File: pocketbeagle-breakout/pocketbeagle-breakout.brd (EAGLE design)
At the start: 102.9 x 68.6 mm, 91 parts, among them J30 4-1734592-04-1734592-0, J31 4-1734592-04-1734592-0, J5 POWER_JACKSLT, P1 BCS-118-L-D-TE, P1IN BCS-118-L-D-TE, P2 BCS-118-L-D-TE, P2IN BCS-118-L-D-TE, U1 TCAN330

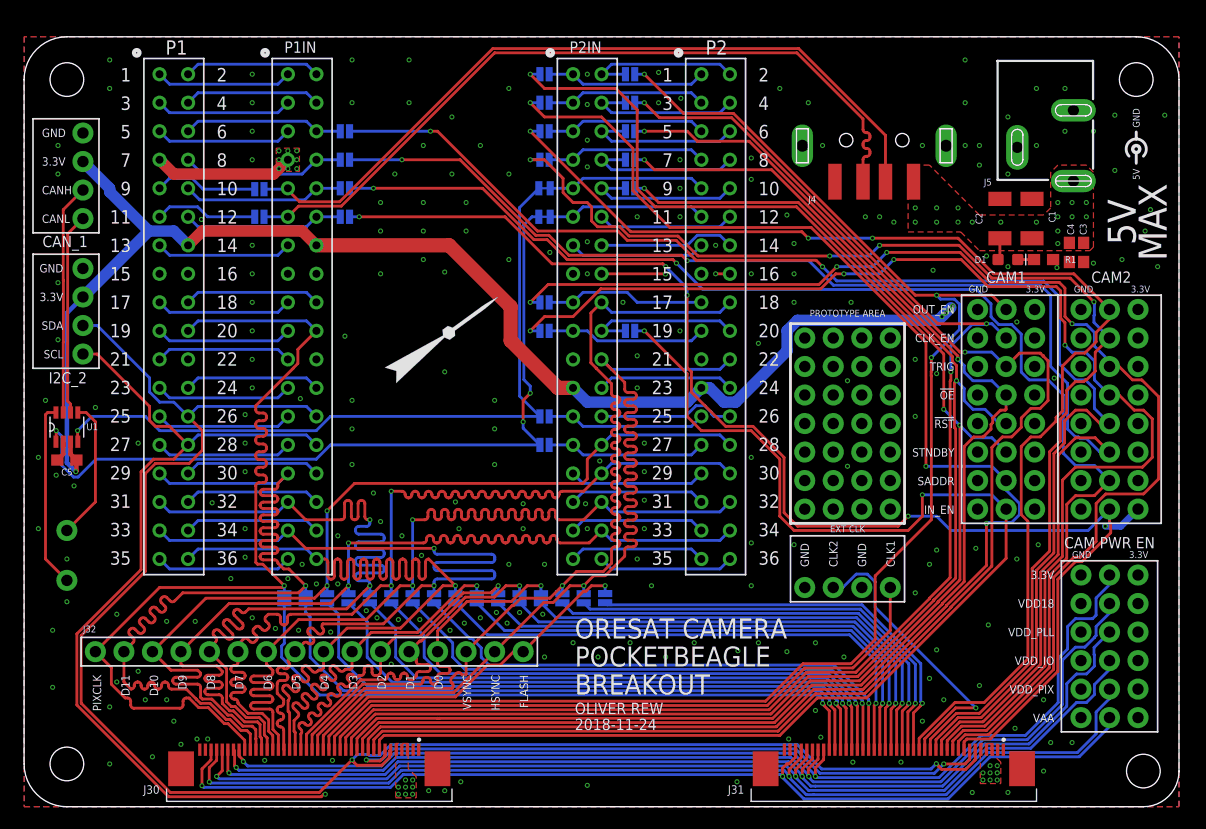
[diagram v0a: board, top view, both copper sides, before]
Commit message: address review comments: used round hole on USB and power, changed CAN connector, other small stuff
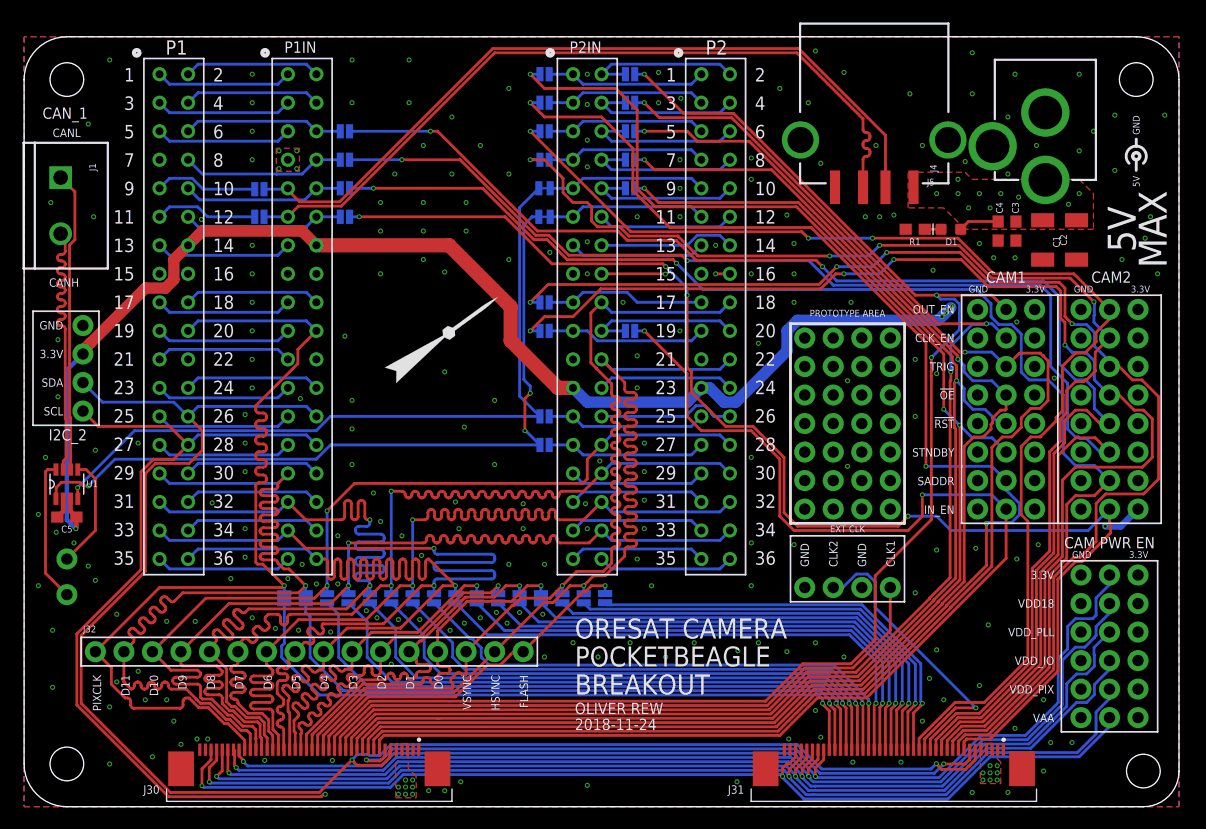
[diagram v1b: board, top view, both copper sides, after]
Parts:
- removed J29: (no value), SparkFun-Connectors:1X04_NO_SILK
- added J1: (no value), SparkFun-Connectors:SCREWTERMINAL-5MM-2
- J4: value (none) -> USB_A_SMT_FEMALE; device J-WURTH-USB-A-FEMALE-629104151021:629104151021 -> SparkFun-Connectors:USB-A-S-SILK-FEMALE
- J5: value POWER_JACKSLT -> POWER_JACK; device SparkFun-Connectors:POWER_JACK_SLOT -> SparkFun-Connectors:POWER_JACK_PTH
- moved R1 11.7 mm to (79.4, 51.4), turned to 180 degrees
- moved C4 6.63 mm to (86.8, 51.3)
- moved C3 6.33 mm to (88.3, 51.3)
- moved D1 5.75 mm to (82.5, 51.4), turned to 180 degrees
- moved J19 5.08 mm to (5.24, 42.9)
- moved C5 5.08 mm to (3.81, 25.8)
- moved J5 5.08 mm to (91.0, 69.5)
- moved U1 5.08 mm to (3.81, 28.7)
- moved C1 4.40 mm to (93.7, 50.5), turned to 270 degrees
- moved C2 4.26 mm to (90.7, 50.5), turned to 270 degrees
- moved J4 3.02 mm to (75.7, 62.4), turned to 270 degrees
- moved J36 2.54 mm to (3.81, 22.1)
- moved J37 1.27 mm to (3.81, 18.9)
- moved U$2 0.63 mm to (99.1, 57.9)
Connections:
- net 3.3V: no longer J29.2
- net 5V: now also J4.VBUS; no longer J4.1
- net CAN_H: now also J1.2; no longer J29.3
- net CAN_L: now also J1.1; no longer J29.4
- net GND: now also J4.GND, J4.SHLD1, J4.SHLD2, J5.GND, J5.GNDBREAK; no longer J29.1, J4.4, J4.SHELL1, J4.SHELL2, J5.GND@1, J5.GND@2
- net USB_D+: now also J4.D+; no longer J4.3
- net USB_D-: now also J4.D-; no longer J4.2
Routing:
- net 5V: track 14.4 -> 3.62 mm, vias 41 -> 30
- net CAN_L: track 18.0 -> 26.8 mm
- net 3.3V: track 144.3 -> 138.4 mm
- net CAN_H: track 20.6 -> 25.7 mm
- net N$19: track 16.6 -> 12.8 mm
- net SCL2: track 143.3 -> 140.5 mm
- net SDA2: track 149.9 -> 147.1 mm
- net N$18: track 12.6 -> 10.1 mm
- net CAN_TX: track 70.6 -> 68.2 mm
- net CAN_RX: track 65.5 -> 66.6 mm
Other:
- board text added: "CAN1 ALT NOT CONNECTED"
- board text added: "CAN1 CONNECTED"
- board text added: "CANH"
- board text added: "CANL"
- board text removed: "GND 3.3V CANH CANL"

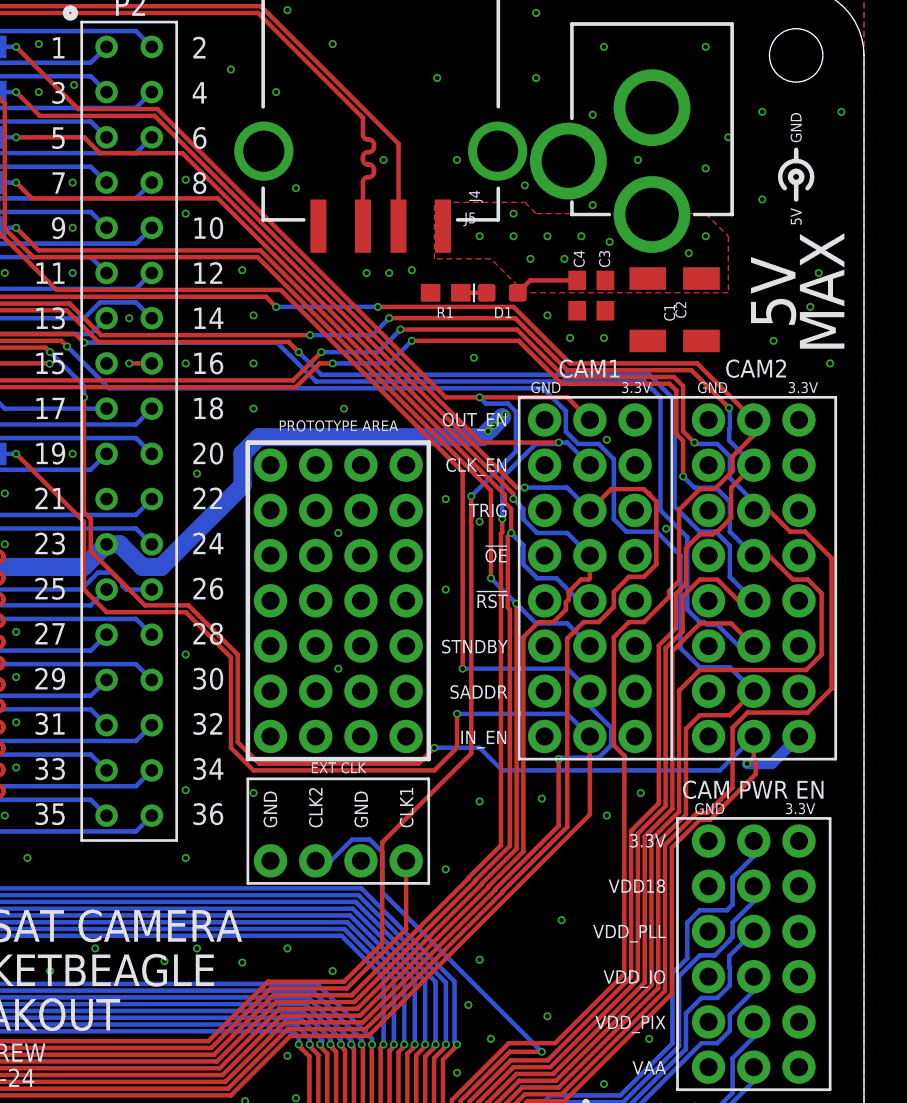
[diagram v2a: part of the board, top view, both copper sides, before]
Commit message: Fixed flow through on layer 15 because OCD.
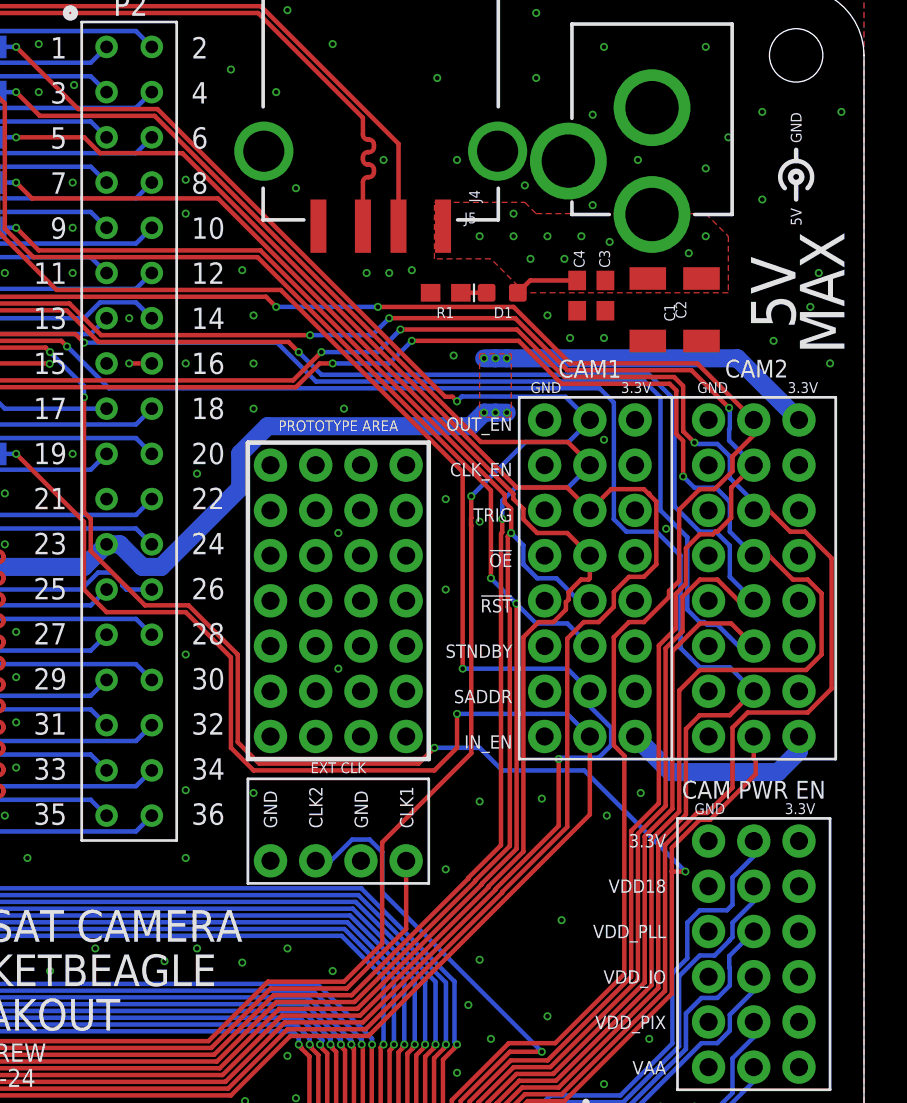
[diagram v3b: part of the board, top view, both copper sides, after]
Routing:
- net 3.3V: track 138.4 -> 147.0 mm, vias 6 -> 7
- net INPUT_DRVR_EN_2: track 117.3 -> 115.8 mm, vias 4 -> 5
- net SADDR_2: track 116.1 -> 117.3 mm
- net OUTPUT_DRVR_EN_1: track 130.0 -> 130.5 mm
- net CLK_EN_1: track 127.3 -> 127.8 mm, vias 3 -> 2
- net TRIG_1: vias 2 -> 1
- net OE_BAR_1: vias 2 -> 1
- added copper zone on layer 1, net 3.3V
